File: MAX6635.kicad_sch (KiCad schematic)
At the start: 2 parts, among them U10 MAX6633MSA_T

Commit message: Fix TCAN power supply swap
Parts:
- C20: DigiKey Part Number (none) -> 720-GA0805Y104JXABT31GCT-ND
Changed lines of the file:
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@@
+			)
+		)
+		(property "DigiKey Part Number" "720-GA0805Y104JXABT31GCT-ND"
+			(at 234.95 115.57 0)
+			(effects
+				(font
+					(size 1.27 1.27)
+				)
+				(hide yes)
 			)
 		)

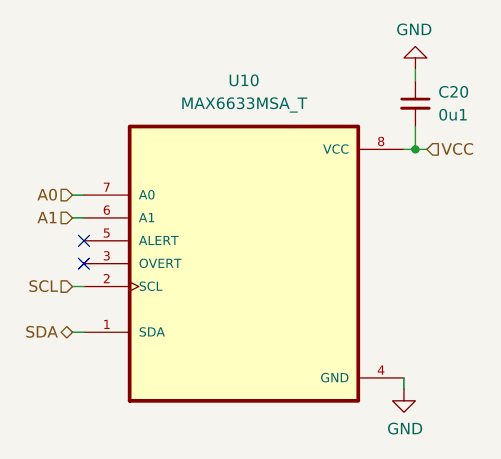
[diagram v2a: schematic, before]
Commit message: Add PCM5102A I2S audio output for APRS radio
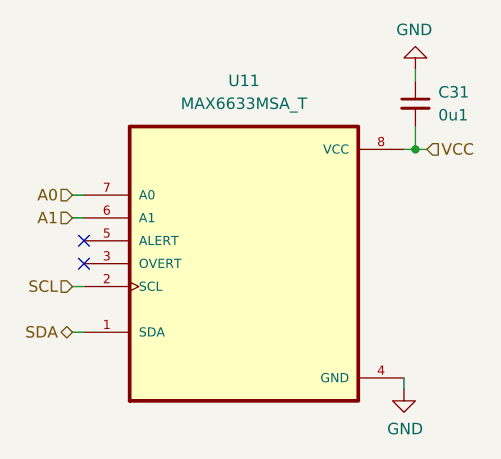
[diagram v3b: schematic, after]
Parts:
- renumbered C20 to C31, U10 to U11
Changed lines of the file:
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@@
 	(generator "eeschema")
 	(generator_version "9.0")
-	(paper "USLedger")
+	(paper "C")
 	(title_block
 		(title "HEDGE-2 OBC")
@@
 		(on_board yes)
 		(dnp no)
-		(property "Reference" "#PWR084"
+		(property "Reference" "#PWR095"
 			(at 233.68 153.67 0)
 			(effects
@@
 			(project "HEDGE2-OBC"
 				(path "/a13a6ce3-91ba-42e3-9b40-443fe6a0f2d9/447e6187-2c4f-4605-bcfa-9c5de09578b6"
-					(reference "#PWR084")
+					(reference "#PWR095")
 					(unit 1)
 				)
@@
 		(dnp no)
 		(fields_autoplaced yes)
-		(property "Reference" "U10"
+		(property "Reference" "U11"
 			(at 215.9 113.03 0)
 			(effects
@@
 			(project "HEDGE2-OBC"
 				(path "/a13a6ce3-91ba-42e3-9b40-443fe6a0f2d9/447e6187-2c4f-4605-bcfa-9c5de09578b6"
-					(reference "U10")
+					(reference "U11")
 					(unit 1)
 				)
@@
 		(dnp no)
 		(fields_autoplaced yes)
-		(property "Reference" "C20"
+		(property "Reference" "C31"
 			(at 237.49 114.3062 0)
 			(effects
@@
 			(project "HEDGE2-OBC"
 				(path "/a13a6ce3-91ba-42e3-9b40-443fe6a0f2d9/447e6187-2c4f-4605-bcfa-9c5de09578b6"
-					(reference "C20")
+					(reference "C31")
 					(unit 1)
 				)
@@
 		(on_board yes)
 		(dnp no)
-		(property "Reference" "#PWR085"
+		(property "Reference" "#PWR096"
 			(at 234.95 105.41 0)
 			(effects
@@
 			(project "HEDGE2-OBC"
 				(path "/a13a6ce3-91ba-42e3-9b40-443fe6a0f2d9/447e6187-2c4f-4605-bcfa-9c5de09578b6"
-					(reference "#PWR085")
+					(reference "#PWR096")
 					(unit 1)
 				)

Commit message: Add PCM and SPI UART; begin layout update
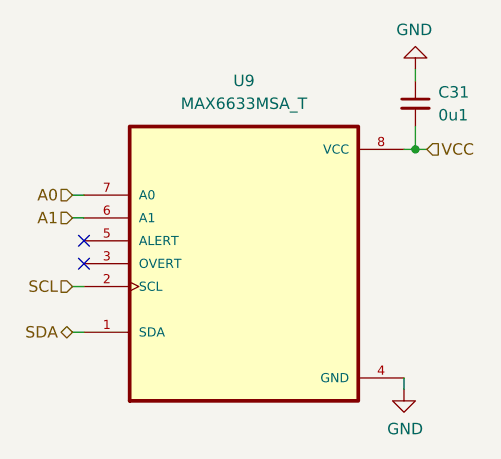
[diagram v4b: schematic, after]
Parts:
- renumbered U11 to U9
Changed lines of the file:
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@@
 		(on_board yes)
 		(dnp no)
-		(property "Reference" "#PWR095"
+		(property "Reference" "#PWR091"
 			(at 233.68 153.67 0)
 			(effects
@@
 			(project "HEDGE2-OBC"
 				(path "/a13a6ce3-91ba-42e3-9b40-443fe6a0f2d9/447e6187-2c4f-4605-bcfa-9c5de09578b6"
-					(reference "#PWR095")
+					(reference "#PWR091")
 					(unit 1)
 				)
@@
 		(dnp no)
 		(fields_autoplaced yes)
-		(property "Reference" "U11"
+		(property "Reference" "U9"
 			(at 215.9 113.03 0)
 			(effects
@@
 			(project "HEDGE2-OBC"
 				(path "/a13a6ce3-91ba-42e3-9b40-443fe6a0f2d9/447e6187-2c4f-4605-bcfa-9c5de09578b6"
-					(reference "U11")
+					(reference "U9")
 					(unit 1)
 				)
@@
 		(on_board yes)
 		(dnp no)
-		(property "Reference" "#PWR096"
+		(property "Reference" "#PWR092"
 			(at 234.95 105.41 0)
 			(effects
@@
 			(project "HEDGE2-OBC"
 				(path "/a13a6ce3-91ba-42e3-9b40-443fe6a0f2d9/447e6187-2c4f-4605-bcfa-9c5de09578b6"
-					(reference "#PWR096")
+					(reference "#PWR092")
 					(unit 1)
 				)

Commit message: Continue layout update
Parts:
- renumbered C31 to C30
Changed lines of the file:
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@@
 		(on_board yes)
 		(dnp no)
-		(property "Reference" "#PWR091"
+		(property "Reference" "#PWR097"
 			(at 233.68 153.67 0)
 			(effects
@@
 			(project "HEDGE2-OBC"
 				(path "/a13a6ce3-91ba-42e3-9b40-443fe6a0f2d9/447e6187-2c4f-4605-bcfa-9c5de09578b6"
-					(reference "#PWR091")
+					(reference "#PWR097")
 					(unit 1)
 				)
@@
 		(dnp no)
 		(fields_autoplaced yes)
-		(property "Reference" "C31"
+		(property "Reference" "C30"
 			(at 237.49 114.3062 0)
 			(effects
@@
 			(project "HEDGE2-OBC"
 				(path "/a13a6ce3-91ba-42e3-9b40-443fe6a0f2d9/447e6187-2c4f-4605-bcfa-9c5de09578b6"
-					(reference "C31")
+					(reference "C30")
 					(unit 1)
 				)
@@
 		(on_board yes)
 		(dnp no)
-		(property "Reference" "#PWR092"
+		(property "Reference" "#PWR098"
 			(at 234.95 105.41 0)
 			(effects
@@
 			(project "HEDGE2-OBC"
 				(path "/a13a6ce3-91ba-42e3-9b40-443fe6a0f2d9/447e6187-2c4f-4605-bcfa-9c5de09578b6"
-					(reference "#PWR092")
+					(reference "#PWR098")
 					(unit 1)
 				)
